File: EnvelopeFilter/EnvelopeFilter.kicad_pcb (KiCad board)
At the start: 2 copper layers, 49.5 x 97.8 mm, 60 parts, among them J1 Conn_01x02_Male, J2 Conn_01x03_Male, J3 Conn_01x03_Male, J4 Conn_01x03_Male, J5 Conn_01x03_Male, J6 Conn_01x03_Male, J7 Conn_01x03_Male, J8 Conn_01x03_Male, J9 Conn_01x09_Male, U1 AS3320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

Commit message: Exported panel, fixed missing net on filter
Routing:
- net Net-(J1-Pad2): track 0.00 -> 4.45 mm
- net GND: vias 27 -> 26

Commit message: Updated PCB annotations
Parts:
- renumbered R11 to C13

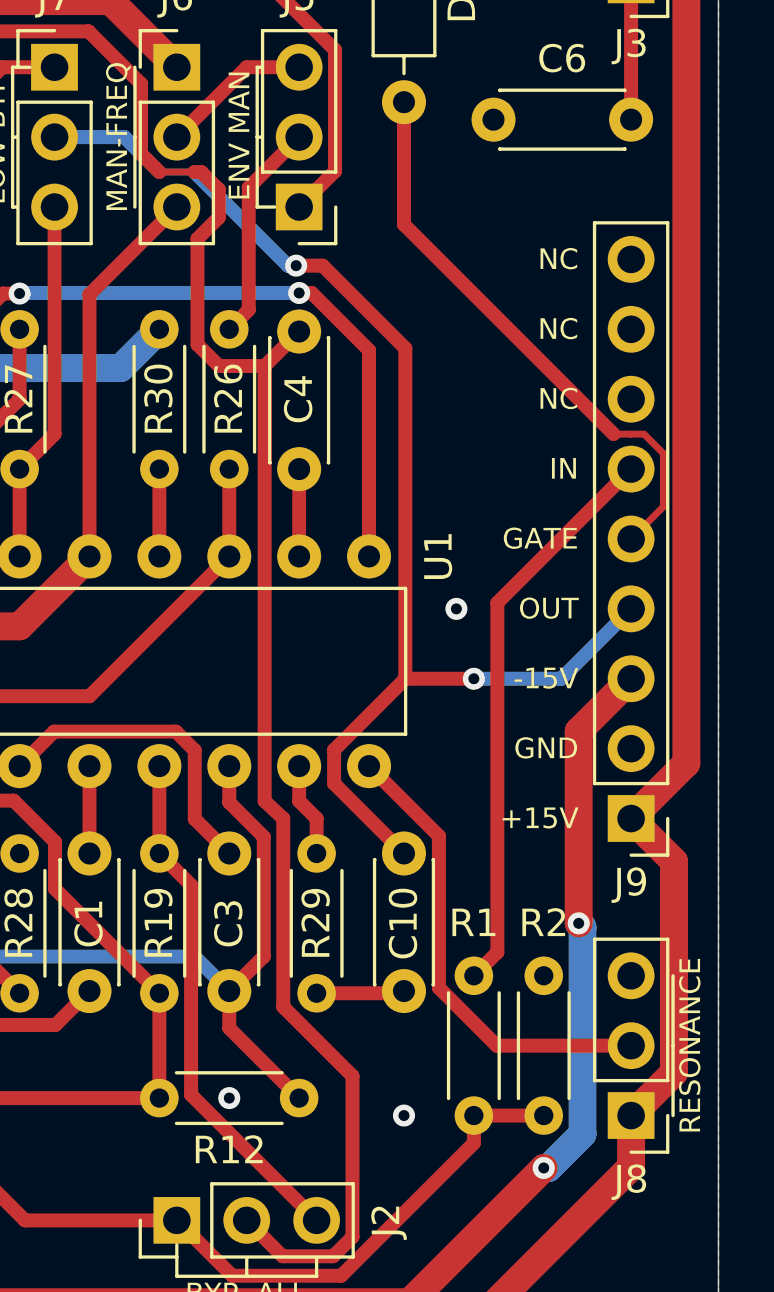
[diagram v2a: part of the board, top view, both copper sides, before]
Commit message: Resolved Issue #3 Also: * Added output cap to 555 modules * EnvelopeFilter now has an output cap
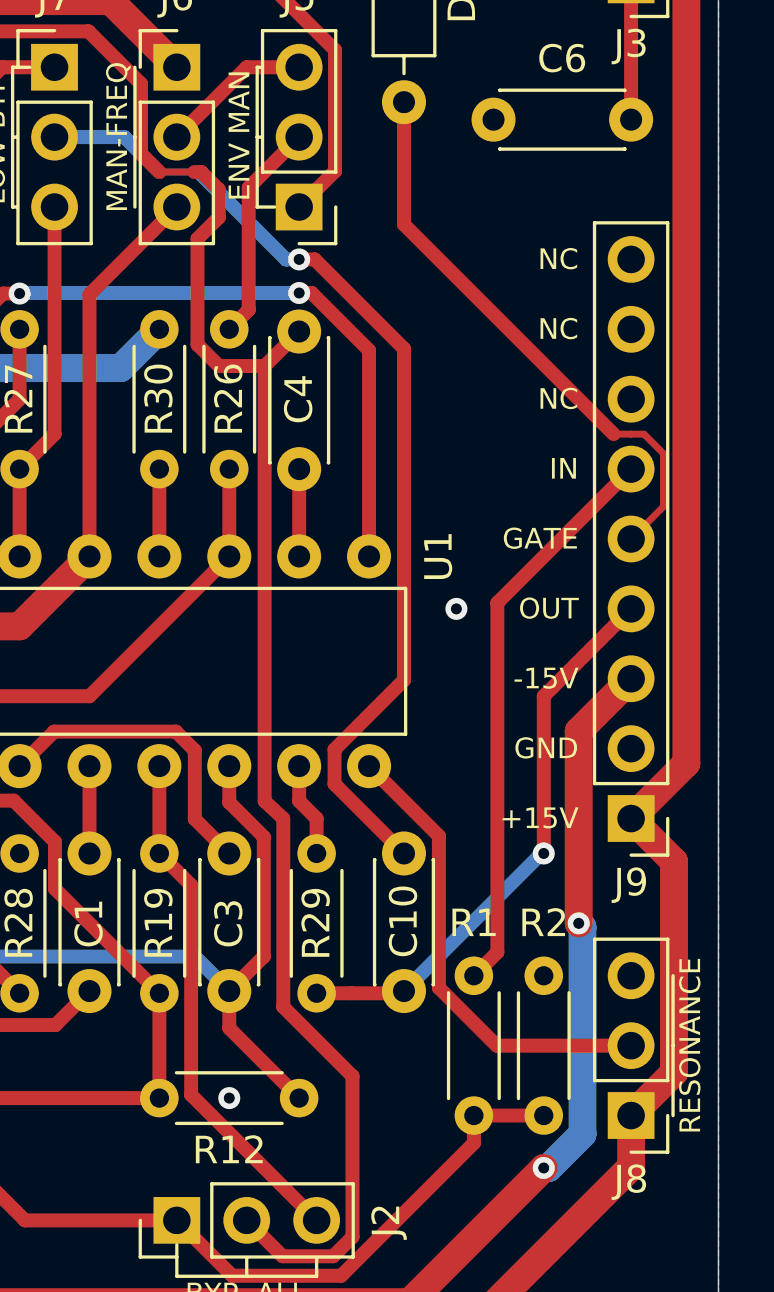
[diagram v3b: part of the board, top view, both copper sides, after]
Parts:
- moved C10 5.00 mm to (165.7, 125.7), turned to 270 degrees
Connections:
- J7 pad 2: /SIG_OUT -> Net-(C10-Pad1)
- R29 pad 2: Net-(C10-Pad1) -> /SIG_OUT
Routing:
- net Net-(C10-Pad1): track 3.21 -> 36.3 mm, vias 0 -> 1
- net /SIG_OUT: track 45.7 -> 20.6 mm, vias 2 -> 1
- net GND: vias 26 -> 25

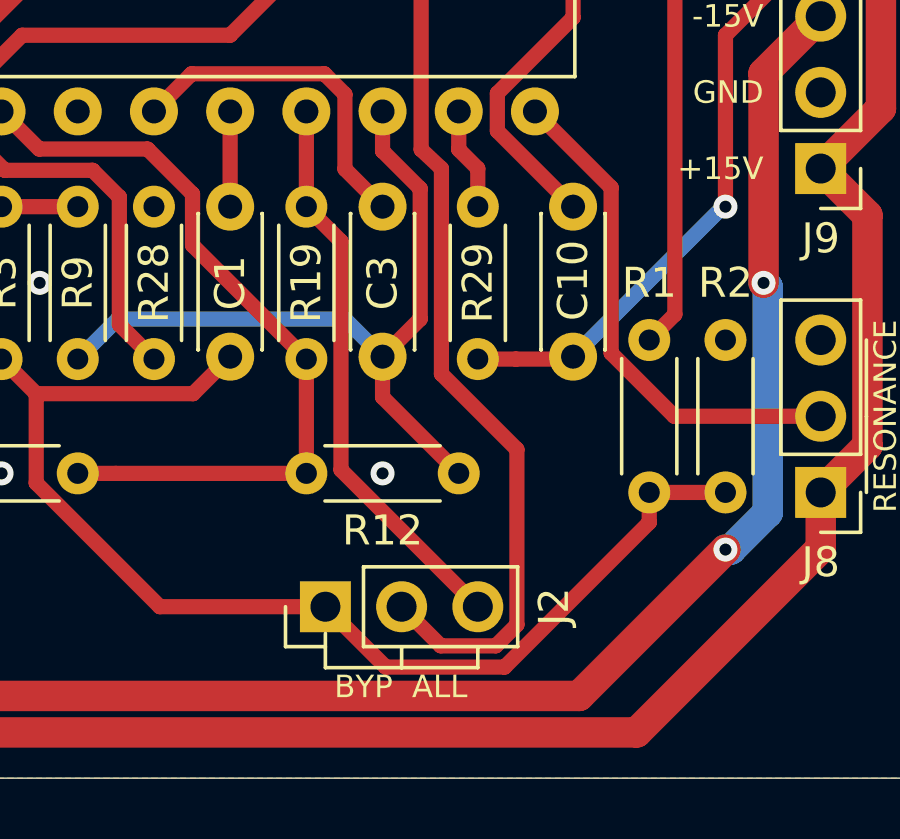
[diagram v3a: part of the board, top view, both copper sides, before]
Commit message: Added resonance current limit resistor
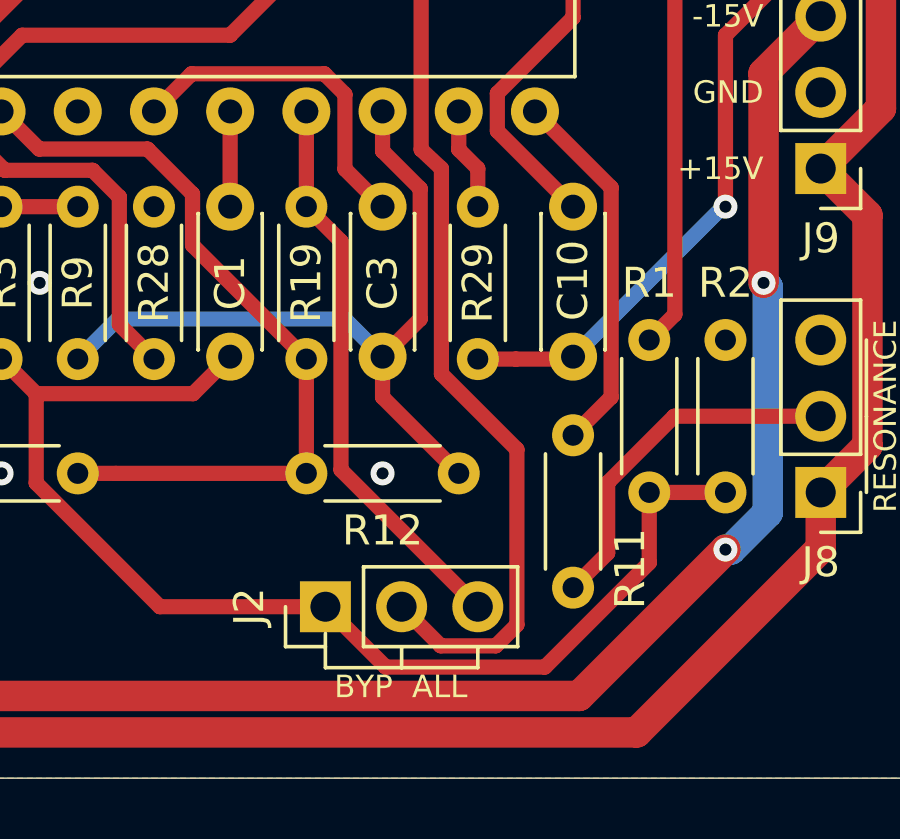
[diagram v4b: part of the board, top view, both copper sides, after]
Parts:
- added R11: 200k, Resistor_THT:R_Axial_DIN0204_L3.6mm_D1.6mm_P5.08mm_Horizontal, F.Cu at (165.7, 133.3)
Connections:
- U1 pad 9: Net-(J8-Pad2) -> Net-(R11-Pad1)
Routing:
- net Net-(R11-Pad1): track 0.00 -> 12.4 mm
- net Net-(J8-Pad2): track 17.0 -> 12.0 mm
- net Net-(C1-Pad1): track 40.1 -> 40.9 mm
